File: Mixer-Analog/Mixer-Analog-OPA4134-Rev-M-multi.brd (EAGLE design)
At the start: 123 x 51 mm, 119 parts, among them IC1 BQ297X, IC2 MCP73831, IC3 QS6K1, IC4 OPA4134D, IC5 SC4503, IC6 TPS7A49, J10 PHONES-OUT, J11 12V, J7 Battery, J9 LINE-OUT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

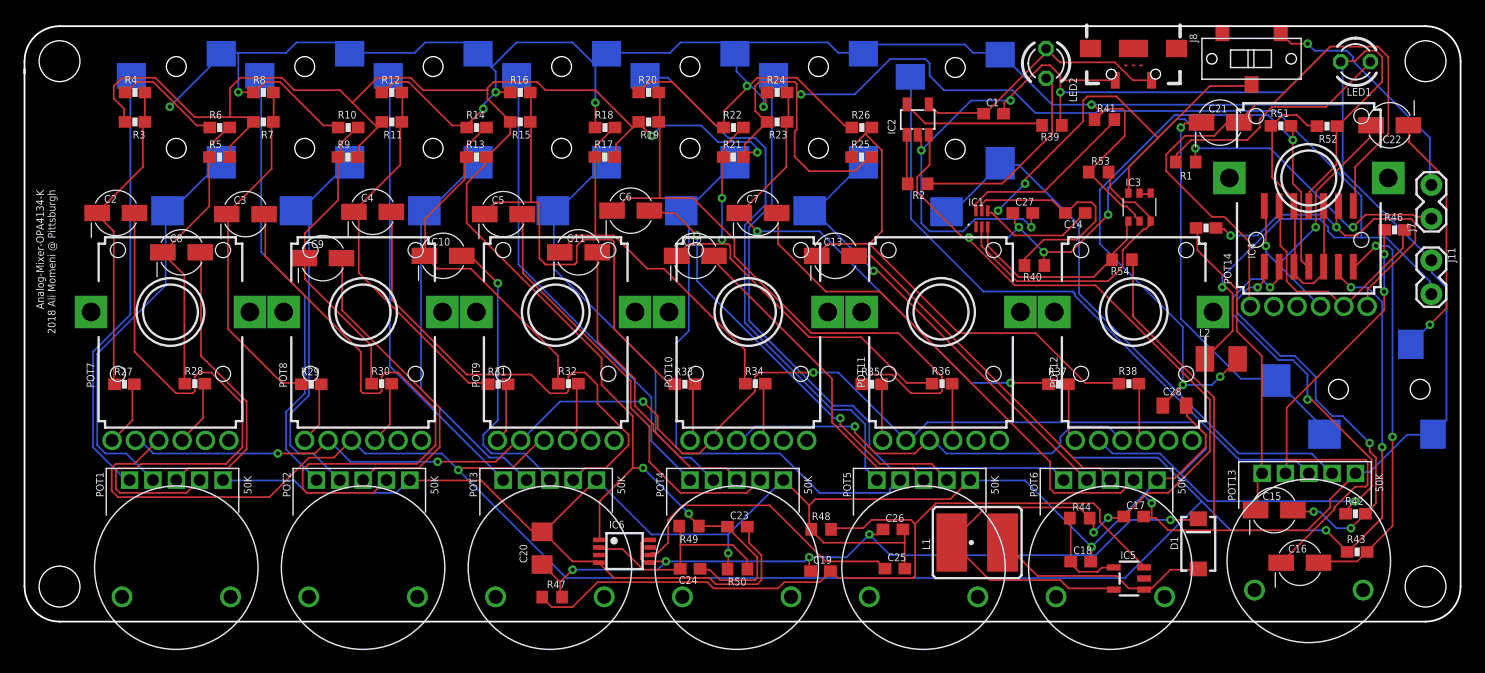
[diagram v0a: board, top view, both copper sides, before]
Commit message: pot reference changed in both boards
The pot side hole size update was not reflected in the boards. now they are referenced to the latest version of the device.
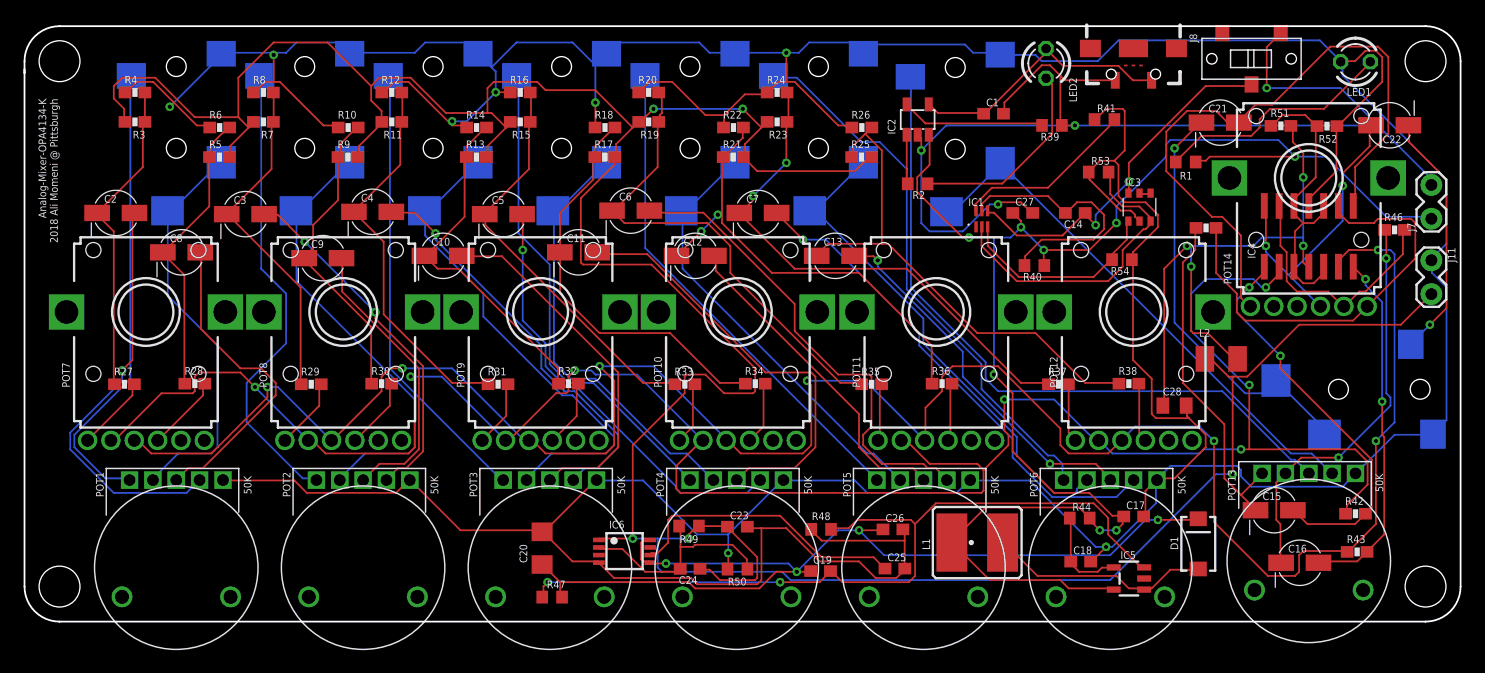
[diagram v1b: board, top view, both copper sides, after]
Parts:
- moved POT7 2.10 mm to (10.4, 26.5)
- moved POT8 1.70 mm to (27.3, 26.5)
- moved POT9 1.30 mm to (44.2, 26.5)
- moved POT10 0.90 mm to (61.1, 26.5)
- moved POT11 0.40 mm to (78.1, 26.5)
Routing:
- net OUT-R: track 212.5 -> 189.9 mm, vias 5 -> 7
- net N$29: track 52.5 -> 30.8 mm, vias 0 -> 2
- net OUT-L: track 165.5 -> 184.0 mm
- net BATGND: track 46.8 -> 32.4 mm
- net N$8: track 49.9 -> 35.6 mm, vias 0 -> 1
- net N$81: track 54.2 -> 41.0 mm
- net V+: track 69.2 -> 82.1 mm, vias 5 -> 4
- net N$80: track 49.2 -> 37.5 mm
- net N$62: track 26.2 -> 37.1 mm
- net N$33: track 60.6 -> 49.8 mm, vias 3 -> 4
- net GND: track 469.1 -> 478.9 mm, vias 11 -> 8
- net USBGND: track 90.6 -> 99.8 mm, vias 5 -> 4
- net OUT-R1: track 43.6 -> 34.8 mm
- net N$46: track 34.0 -> 42.4 mm
- net N$92: track 55.7 -> 47.3 mm
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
